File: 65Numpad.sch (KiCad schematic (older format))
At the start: 174 parts, among them J1 MX-NoLED, K1 MX-NoLED, M1 MX-NoLED, P1 MX-NoLED, Q1 MX-NoLED, T1 MX-NoLED, U2 MX-NoLED, X1 MX-NoLED, Y1 MX-NoLED

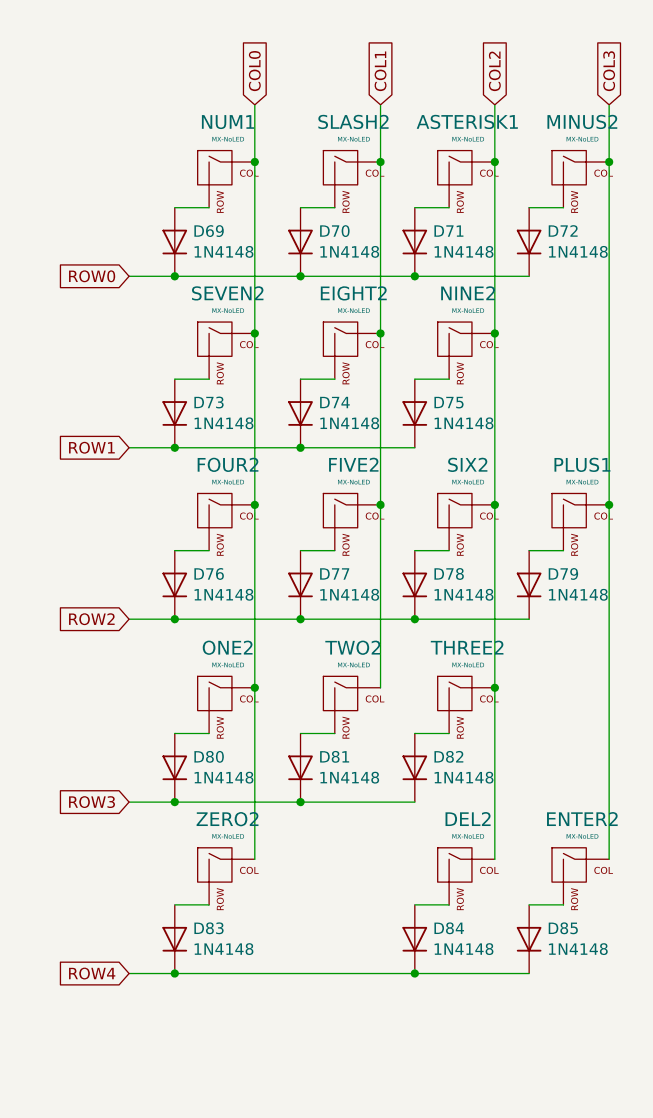
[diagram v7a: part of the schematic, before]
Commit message: Removed traces
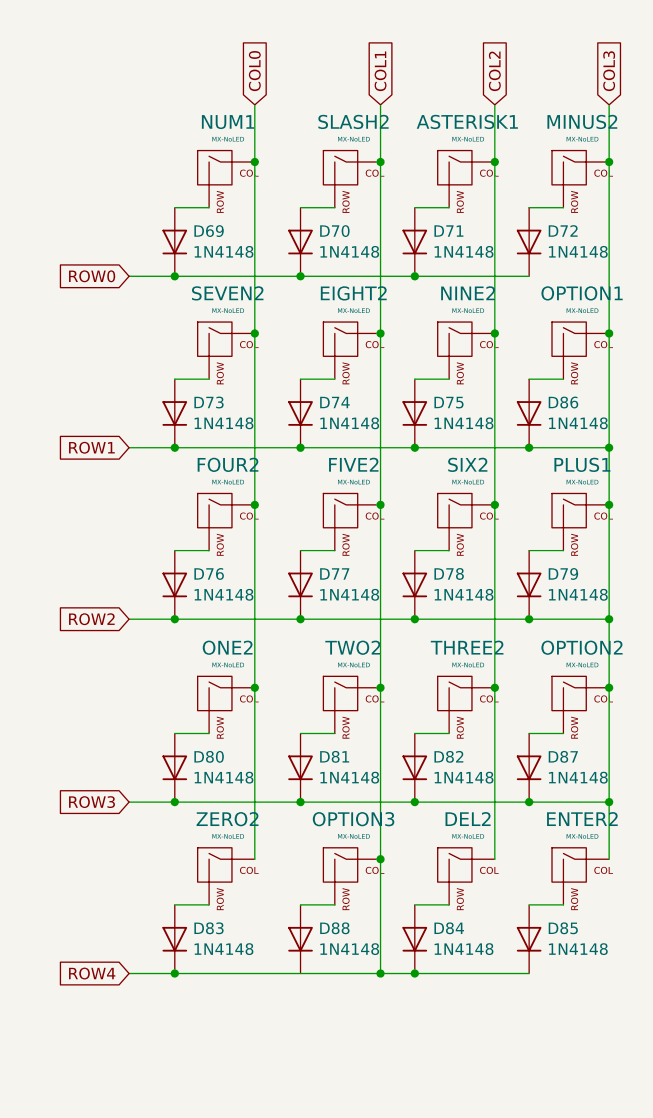
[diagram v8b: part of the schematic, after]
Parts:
- added D86, D87, D88: 1N4148, Diodes_THT:D_DO-35_SOD27_P7.62mm_Horizontal, symbol Diode:1N4148
- added OPTION1, OPTION2, OPTION3: MX-NoLED, MX_Only:MXOnly-1U-NoLEDHotswap, symbol MX_Alps_Hybrid:MX-NoLED
- POGO1, POGO3: footprint Pin_Headers:Pin_Header_Angled_1x04_Pitch2.54mm -> 65Numpad:PogoConnector
- POGO2, POGO4: footprint Pin_Headers:Pin_Header_Angled_1x04_Pitch2.54mm -> 65Numpad:PogoConnectorMirrored
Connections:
- net ROW1 is gone; now on net COL3: D10.1 (K), D12.1 (K), D14.1 (K), D2.1 (K), D4.1 (K), D6.1 (K), D73.1 (K), D74.1 (K), D75.1 (K), D8.1 (K), Main1.18 (A1/PF6), Numpad1.7 (4/PD4)
- net ROW2 is gone; now on net COL3: D15.1 (K), D17.1 (K), D19.1 (K), D21.1 (K), D23.1 (K), D25.1 (K), D27.1 (K), D76.1 (K), D77.1 (K), D78.1 (K), D79.1 (K), Main1.17 (A0/PF7), Numpad1.8 (5/PC6)
- net ROW3 is gone; now on net COL3: D16.1 (K), D18.1 (K), D20.1 (K), D22.1 (K), D24.1 (K), D26.1 (K), D28.1 (K), D80.1 (K), D81.1 (K), D82.1 (K), Main1.16 (15/PB1), Numpad1.9 (6/PD7)
- net ROW4 is gone; now on net COL1: D30.1 (K), D32.1 (K), D34.1 (K), D36.1 (K), D38.1 (K), D40.1 (K), D42.1 (K), D83.1 (K), D84.1 (K), D85.1 (K), Main1.14 (16/PB2), Numpad1.10 (7/PE6)
- net COL1: now also OPTION3.1 (COL)
- net COL3: now also D86.1 (K), D87.1 (K), OPTION1.1 (COL), OPTION2.1 (COL)
- new net: D86.2 (A), OPTION1.2 (ROW)
- new net: D87.2 (A), OPTION2.2 (ROW)
- new net: D88.2 (A), OPTION3.2 (ROW)
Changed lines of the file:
@@
 F 0 "POGO1" H 3230 992 50  0000 L CNN
 F 1 "Conn_01x04" H 3230 901 50  0000 L CNN
-F 2 "Pin_Headers:Pin_Header_Angled_1x04_Pitch2.54mm" H 3150 1000 50  0001 C CNN
+F 2 "65Numpad:PogoConnector" H 3150 1000 50  0001 C CNN
 F 3 "~" H 3150 1000 50  0001 C CNN
 	1    3150 1000
@@
 F 0 "POGO2" H 4330 992 50  0000 L CNN
 F 1 "Conn_01x04" H 4330 901 50  0000 L CNN
-F 2 "Pin_Headers:Pin_Header_Angled_1x04_Pitch2.54mm" H 4250 1000 50  0001 C CNN
+F 2 "65Numpad:PogoConnectorMirrored" H 4250 1000 50  0001 C CNN
 F 3 "~" H 4250 1000 50  0001 C CNN
 	1    4250 1000
@@
 F 0 "POGO3" H 15230 892 50  0000 L CNN
 F 1 "Conn_01x04" H 15230 801 50  0000 L CNN
-F 2 "Pin_Headers:Pin_Header_Angled_1x04_Pitch2.54mm" H 15150 900 50  0001 C CNN
+F 2 "65Numpad:PogoConnector" H 15150 900 50  0001 C CNN
 F 3 "~" H 15150 900 50  0001 C CNN
 	1    15150 900
@@
 F 0 "POGO4" H 16330 892 50  0000 L CNN
 F 1 "Conn_01x04" H 16330 801 50  0000 L CNN
-F 2 "Pin_Headers:Pin_Header_Angled_1x04_Pitch2.54mm" H 16250 900 50  0001 C CNN
+F 2 "65Numpad:PogoConnectorMirrored" H 16250 900 50  0001 C CNN
 F 3 "~" H 16250 900 50  0001 C CNN
 	1    16250 900
@@
 Connection ~ 16100 5600
 Wire Wire Line
-	16100 5600 15050 5600
+	16100 5600 15950 5600
 Wire Wire Line
 	15400 5100 15400 4350
@@
 Connection ~ 16950 2050
 Wire Wire Line
-	16950 2050 16950 3550
+	16950 2050 16950 2800
 Connection ~ 16950 3550
 Wire Wire Line
-	16950 3550 16950 5100
+	16950 3550 16950 4050
 Text GLabel 14850 2550 0    50   Input ~ 0
 ROW0
@@
 Text GLabel 13900 1650 2    50   Input ~ 0
 COL3
+Wire Wire Line
+	16750 3000 16600 3000
+$Comp
+L Diode:1N4148 D86
+U 1 1 60153E81
+P 16600 3150
+AR Path="/60153E81" Ref="D86"  Part="1"
+AR Path="/6009603F/60153E81" Ref="D?"  Part="1"
+F 0 "D86" V 16646 3071 50  0000 R CNN
+F 1 "1N4148" V 16555 3071 50  0000 R CNN
+F 2 "Diodes_THT:D_DO-35_SOD27_P7.62mm_Horizontal" H 16600 2975 50  0001 C CNN
+F 3 "https://assets.nexperia.com/documents/data-sheet/1N4148_1N4448.pdf" H 16600 3150 50  0001 C CNN
+	1    16600 3150
+	0    -1   -1   0
+$EndComp
+$Comp
+L MX_Alps_Hybrid:MX-NoLED OPTION1
+U 1 1 60153E87
+P 16800 2850
+AR Path="/60153E87" Ref="OPTION1"  Part="1"
+AR Path="/6009603F/60153E87" Ref="OPTION?"  Part="1"
+F 0 "OPTION1" H 16833 3073 60  0000 C CNN
+F 1 "MX-NoLED" H 16833 2999 20  0000 C CNN
+F 2 "MX_Only:MXOnly-1U-NoLEDHotswap" H 16175 2825 60  0001 C CNN
+F 3 "" H 16175 2825 60  0001 C CNN
+	1    16800 2850
+	1    0    0    -1
+$EndComp
+Wire Wire Line
+	16750 4550 16600 4550
+$Comp
+L Diode:1N4148 D87
+U 1 1 6017218A
+P 16600 4700
+AR Path="/6017218A" Ref="D87"  Part="1"
+AR Path="/6009603F/6017218A" Ref="D?"  Part="1"
+F 0 "D87" V 16646 4621 50  0000 R CNN
+F 1 "1N4148" V 16555 4621 50  0000 R CNN
+F 2 "Diodes_THT:D_DO-35_SOD27_P7.62mm_Horizontal" H 16600 4525 50  0001 C CNN
+F 3 "https://assets.nexperia.com/documents/data-sheet/1N4148_1N4448.pdf" H 16600 4700 50  0001 C CNN
+	1    16600 4700
+	0    -1   -1   0
+$EndComp
+$Comp
+L MX_Alps_Hybrid:MX-NoLED OPTION2
+U 1 1 60172190
+P 16800 4400
+AR Path="/60172190" Ref="OPTION2"  Part="1"
+AR Path="/6009603F/60172190" Ref="OPTION?"  Part="1"
+F 0 "OPTION2" H 16833 4623 60  0000 C CNN
+F 1 "MX-NoLED" H 16833 4549 20  0000 C CNN
+F 2 "MX_Only:MXOnly-1U-NoLEDHotswap" H 16175 4375 60  0001 C CNN
+F 3 "" H 16175 4375 60  0001 C CNN
+	1    16800 4400
+	1    0    0    -1
+$EndComp
+Wire Wire Line
+	15750 5300 15600 5300
+$Comp
+L Diode:1N4148 D88
+U 1 1 60190244
+P 15600 5450
+AR Path="/60190244" Ref="D88"  Part="1"
+AR Path="/6009603F/60190244" Ref="D?"  Part="1"
+F 0 "D88" V 15646 5371 50  0000 R CNN
+F 1 "1N4148" V 15555 5371 50  0000 R CNN
+F 2 "Diodes_THT:D_DO-35_SOD27_P7.62mm_Horizontal" H 15600 5275 50  0001 C CNN
+F 3 "https://assets.nexperia.com/documents/data-sheet/1N4148_1N4448.pdf" H 15600 5450 50  0001 C CNN
+	1    15600 5450
+	0    -1   -1   0
+$EndComp
+$Comp
+L MX_Alps_Hybrid:MX-NoLED OPTION3
+U 1 1 6019024A
+P 15800 5150
+AR Path="/6019024A" Ref="OPTION3"  Part="1"
+AR Path="/6009603F/6019024A" Ref="OPTION?"  Part="1"
+F 0 "OPTION3" H 15833 5373 60  0000 C CNN
+F 1 "MX-NoLED" H 15833 5299 20  0000 C CNN
+F 2 "MX_Only:MXOnly-1U-NoLEDHotswap" H 15175 5125 60  0001 C CNN
+F 3 "" H 15175 5125 60  0001 C CNN
+	1    15800 5150
+	1    0    0    -1
+$EndComp
+Wire Wire Line
+	15950 4350 15950 5100
+Connection ~ 15950 4350
+Connection ~ 15950 5600
+Wire Wire Line
+	15950 5600 15050 5600
+Connection ~ 15950 5100
+Wire Wire Line
+	15950 5100 15950 5600
+Wire Wire Line
+	16100 4850 16600 4850
+Connection ~ 16100 4850
+Connection ~ 16950 4850
+Wire Wire Line
+	16950 4850 16950 5100
+Connection ~ 16600 4850
+Wire Wire Line
+	16600 4850 16950 4850
+Wire Wire Line
+	16100 3300 16600 3300
+Connection ~ 16100 3300
+Connection ~ 16950 3300
+Wire Wire Line
+	16950 3300 16950 3550
+Connection ~ 16600 3300
+Wire Wire Line
+	16600 3300 16950 3300
+Connection ~ 16950 2800
+Wire Wire Line
+	16950 2800 16950 3300
+Connection ~ 16950 4350
+Wire Wire Line
+	16950 4350 16950 4850
+Wire Wire Line
+	16600 4050 16950 4050
+Connection ~ 16600 4050
+Connection ~ 16950 4050
+Wire Wire Line
+	16950 4050 16950 4350
 $EndSCHEMATC
